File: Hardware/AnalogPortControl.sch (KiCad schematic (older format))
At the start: 28 parts, among them J10 A1, J11 A2, J12 A3, J13 A4, J14 A5, J9 A0, U3 Buffer, U6 Buffer, U7 DAC

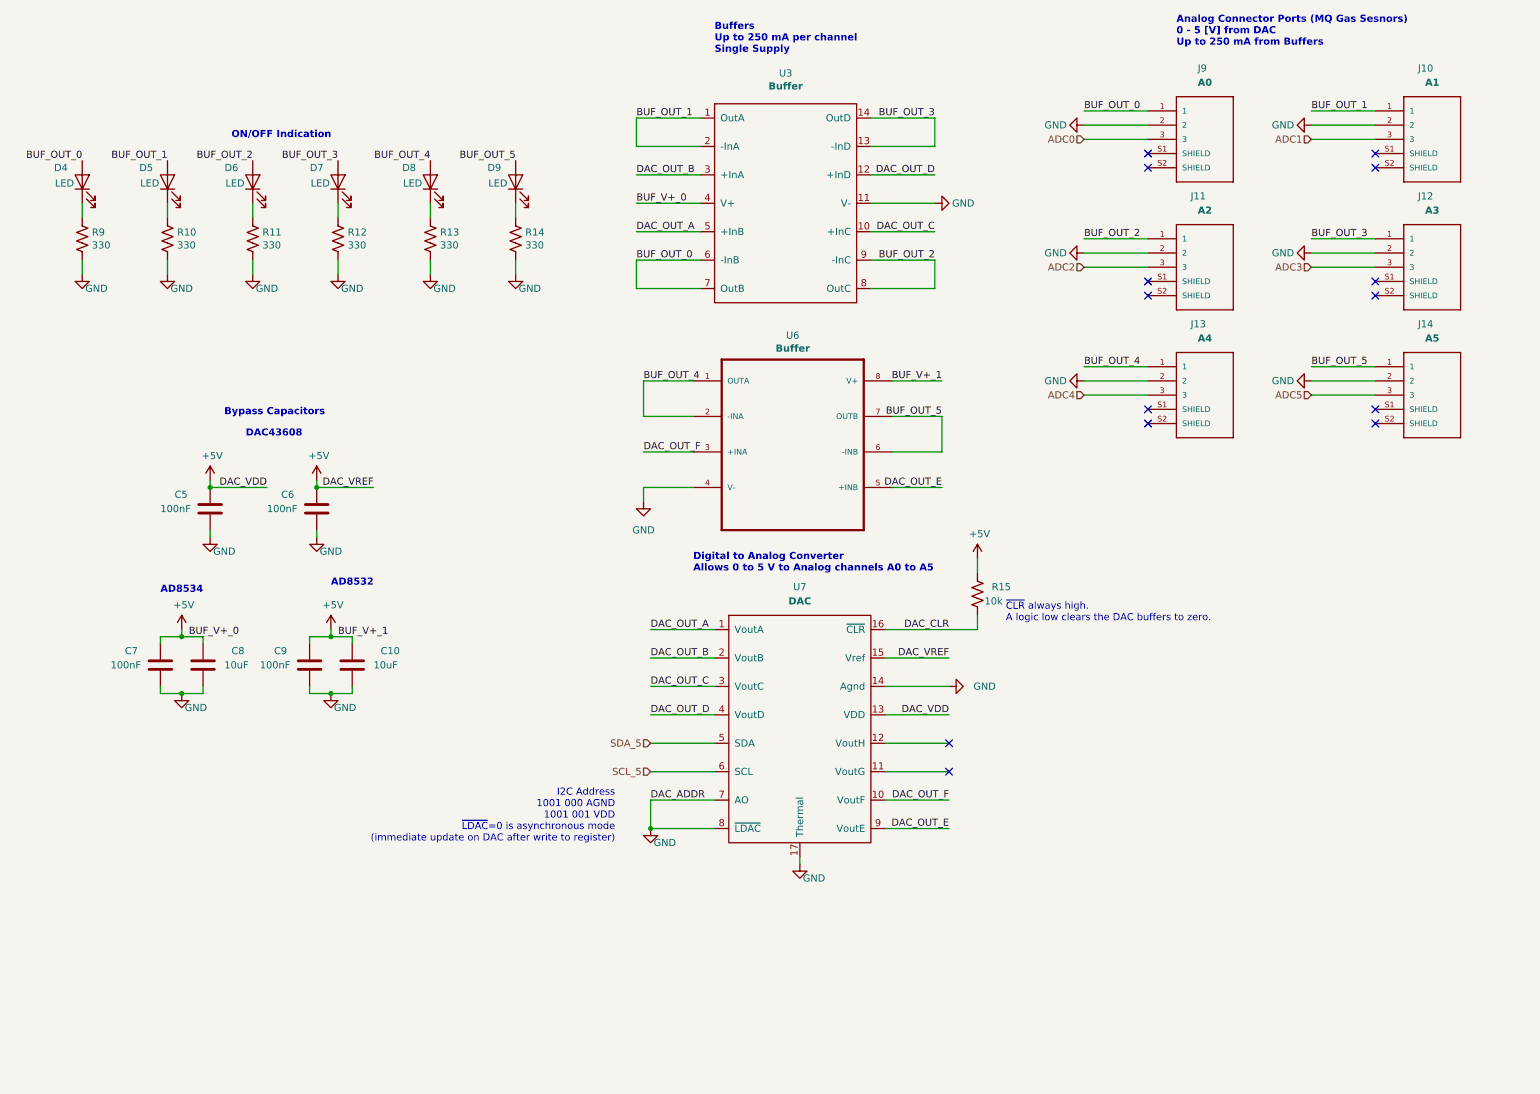
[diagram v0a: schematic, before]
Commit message: Organized Schematic Naming and Added Comments
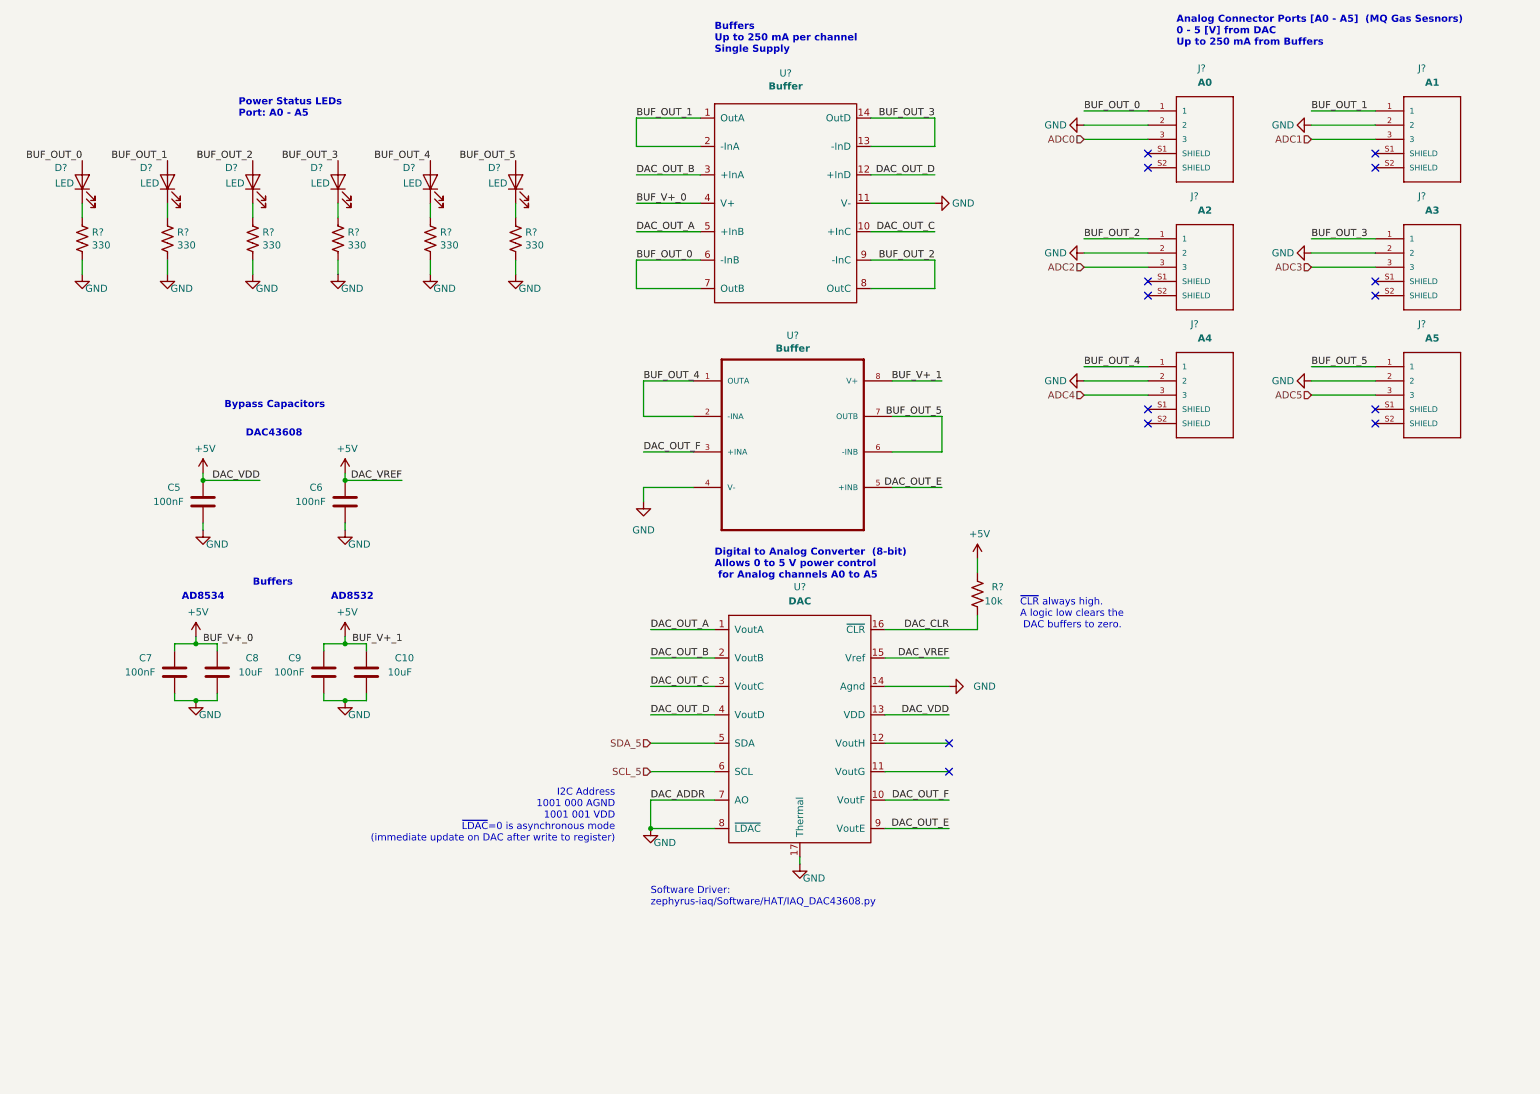
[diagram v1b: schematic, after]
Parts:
- renumbered D4 to D?, D5 to D?, D6 to D?, D7 to D?, D8 to D?, D9 to D?, J9 to J?, J10 to J?, J11 to J?, J12 to J?, J13 to J?, J14 to J?, R9 to R?, R10 to R?, R11 to R?, R12 to R?, R13 to R?, R14 to R?, R15 to R?, U7 to U?, U3 to U?, U6 to U?
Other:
- note added: "Analog Connector Ports [A0 - A5] (MQ Gas Sesnors)\n0 - 5 [V] from DAC\nUp to 250 mA from Buffers"
- note added: "Buffers"
- note added: "Digital to Analog Converter (8-bit)\nAllows 0 to 5 V power control\n for Analog channels A0 to A5"
- note added: "Power Status LEDs\nPort: A0 - A5"
- note added: "Software Driver:\nzephyrus-iaq/Software/HAT/IAQ_DAC43608.py"
- note added: "~CLR~ always high.\nA logic low clears the \n DAC buffers to zero."
- note removed: "Analog Connector Ports (MQ Gas Sesnors)\n0 - 5 [V] from DAC\nUp to 250 mA from Buffers"
- note removed: "Digital to Analog Converter\nAllows 0 to 5 V to Analog channels A0 to A5"
- note removed: "ON/OFF Indication"
- note removed: "~CLR~ always high.\nA logic low clears the DAC buffers to zero."
- moved on the sheet: C10, C5, C6, C7, C8, C9

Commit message: Up Changed I2C addres for DAC and ADC.  Added MOSFET to USART RX.
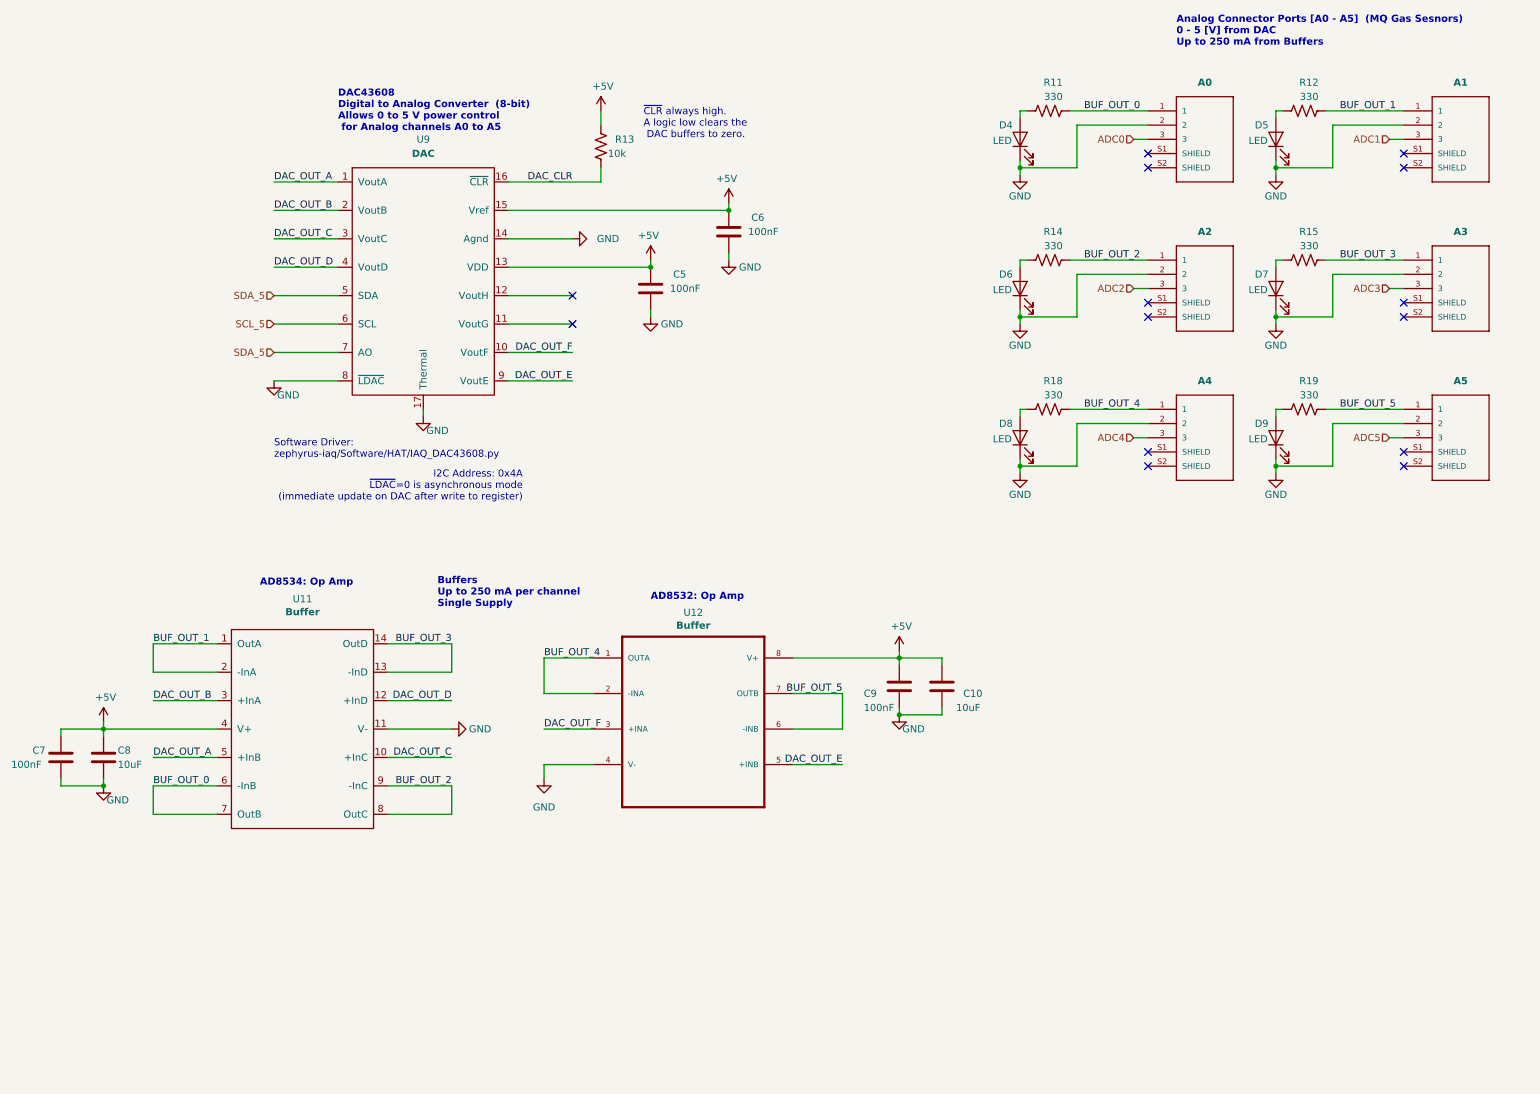
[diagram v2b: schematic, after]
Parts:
- removed D? (x5): LED, Diode_SMD:D_0805_2012Metric, symbol zephyrus_iaq:LED
- removed J?: A1, zephyrus-iaq:JST_SM03B-SRSS-TB(LF)(SN), symbol zephyrus_iaq:SM03B-SRSS-TB(LF)(SN)
- removed J?: A2, zephyrus-iaq:JST_SM03B-SRSS-TB(LF)(SN), symbol zephyrus_iaq:SM03B-SRSS-TB(LF)(SN)
- removed J?: A3, zephyrus-iaq:JST_SM03B-SRSS-TB(LF)(SN), symbol zephyrus_iaq:SM03B-SRSS-TB(LF)(SN)
- removed J?: A4, zephyrus-iaq:JST_SM03B-SRSS-TB(LF)(SN), symbol zephyrus_iaq:SM03B-SRSS-TB(LF)(SN)
- removed J?: A5, zephyrus-iaq:JST_SM03B-SRSS-TB(LF)(SN), symbol zephyrus_iaq:SM03B-SRSS-TB(LF)(SN)
- removed R? (x5): 330, Resistor_SMD:R_0805_2012Metric, symbol zephyrus_iaq:R_US
- added D5, D6, D7, D8, D9: LED, Diode_SMD:D_0805_2012Metric, symbol zephyrus_iaq:LED
- added J11: A1, zephyrus-iaq:JST_SM03B-SRSS-TB(LF)(SN), symbol zephyrus_iaq:SM03B-SRSS-TB(LF)(SN)
- added J12: A2, zephyrus-iaq:JST_SM03B-SRSS-TB(LF)(SN), symbol zephyrus_iaq:SM03B-SRSS-TB(LF)(SN)
- added J13: A3, zephyrus-iaq:JST_SM03B-SRSS-TB(LF)(SN), symbol zephyrus_iaq:SM03B-SRSS-TB(LF)(SN)
- added J14: A4, zephyrus-iaq:JST_SM03B-SRSS-TB(LF)(SN), symbol zephyrus_iaq:SM03B-SRSS-TB(LF)(SN)
- added J15: A5, zephyrus-iaq:JST_SM03B-SRSS-TB(LF)(SN), symbol zephyrus_iaq:SM03B-SRSS-TB(LF)(SN)
- added R12, R14, R15, R18, R19: 330, Resistor_SMD:R_0805_2012Metric, symbol zephyrus_iaq:R_US
- gave numbers to parts that had none: 7
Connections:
- net ADC1: now also J11.3
- net ADC2: now also J12.3
- net ADC3: now also J13.3
- net ADC4: now also J14.3
- net ADC5: now also J15.3
- net BUF_OUT_0: now also R11.2; no longer D4.2 (A)
- net BUF_OUT_1: now also J11.1, R12.2
- net BUF_OUT_2: now also J12.1, R14.2
- net BUF_OUT_3: now also J13.1, R15.2
- net BUF_OUT_4: now also J14.1, R18.2
- net BUF_OUT_5: now also J15.1, R19.2
- net GND: now also D4.1 (K), D5.1 (K), D6.1 (K), D7.1 (K), D8.1 (K), D9.1 (K), J11.2, J12.2, J13.2, J14.2, J15.2; no longer R11.2, U9.7 (AO)
- net SDA_5: now also U9.7 (AO)
- net at R11.1: now also D4.2 (A); no longer D4.1 (K)
- new net: D5.2 (A), R12.1
- new net: D6.2 (A), R14.1
- new net: D7.2 (A), R15.1
- new net: D8.2 (A), R18.1
- new net: D9.2 (A), R19.1
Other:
- note added: "AD8532: Op Amp"
- note added: "AD8534: Op Amp"
- note added: "DAC43608\nDigital to Analog Converter (8-bit)\nAllows 0 to 5 V power control\n for Analog channels A0 to A5"
- note added: "I2C Address: 0x4A\n~LDAC~=0 is asynchronous mode\n(immediate update on DAC after write to register)"
- note removed: "AD8532"
- note removed: "AD8534"
- note removed: "Buffers"
- note removed: "Bypass Capacitors"
- note removed: "DAC43608"
- note removed: "Digital to Analog Converter (8-bit)\nAllows 0 to 5 V power control\n for Analog channels A0 to A5"
- note removed: "I2C Address\n1001 000 AGND\n1001 001 VDD\n~LDAC~=0 is asynchronous mode\n(immediate update on DAC after write to register)"
- note removed: "Power Status LEDs\nPort: A0 - A5"
- moved on the sheet: C10, C5, C6, C7, C8, C9, D4, R11, R13, U11, U12, U9

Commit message: Updated Schematic Attribution and Documentation
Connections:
- net labels removed: DAC_CLR
- wire segments 120 -> 113
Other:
- moved on the sheet: C10, C5, C6, C7, C8, C9, D4, D5, D6, D7, D8, D9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
